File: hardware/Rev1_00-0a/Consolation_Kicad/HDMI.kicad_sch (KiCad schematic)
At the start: 13 parts, among them J1 0484050003, U3 AP2192AFGEG-7

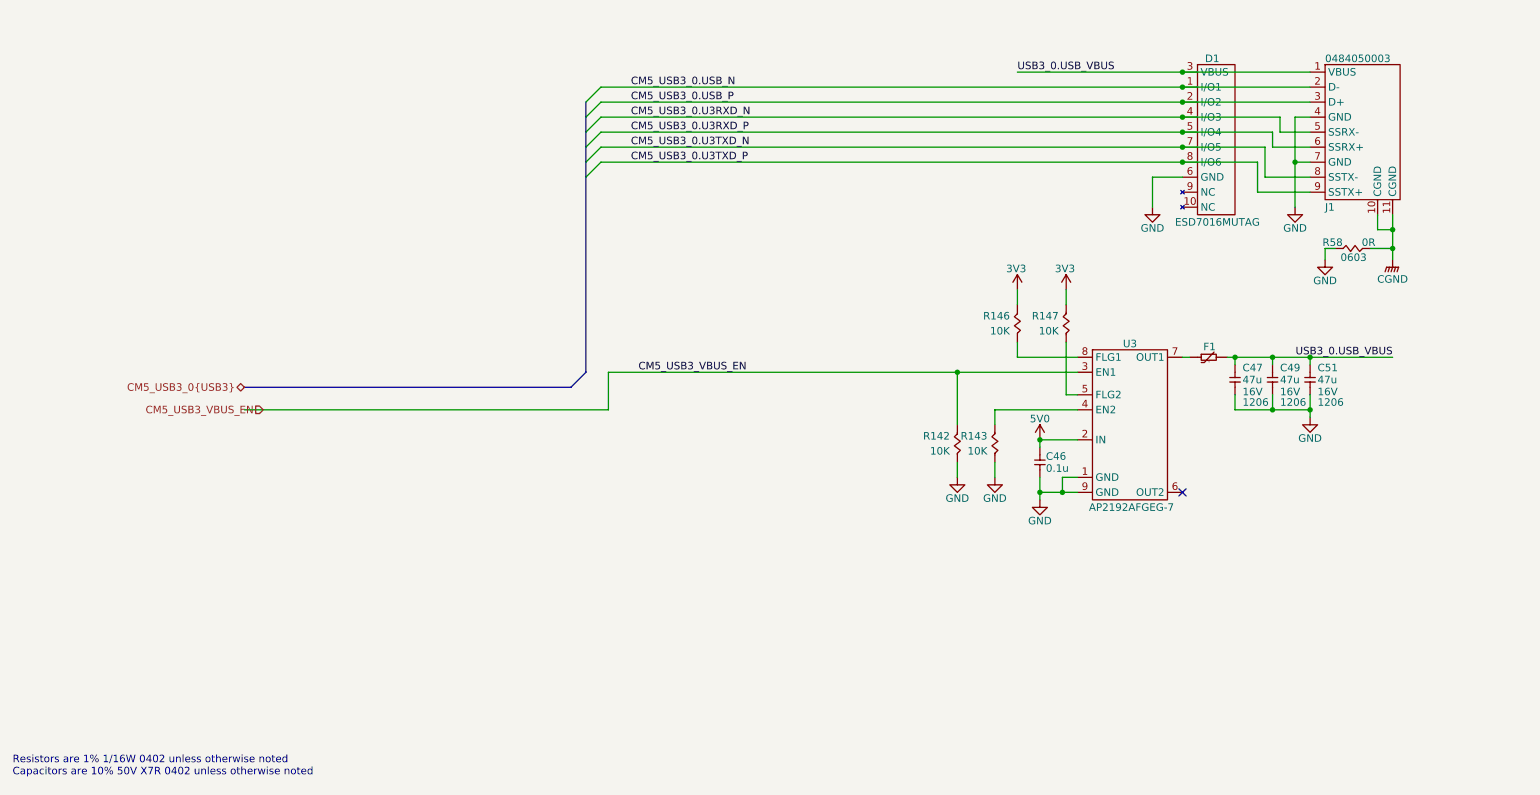
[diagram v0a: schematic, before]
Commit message: Add part number of codec to block diagram Add codec and hdmi schematic sheets
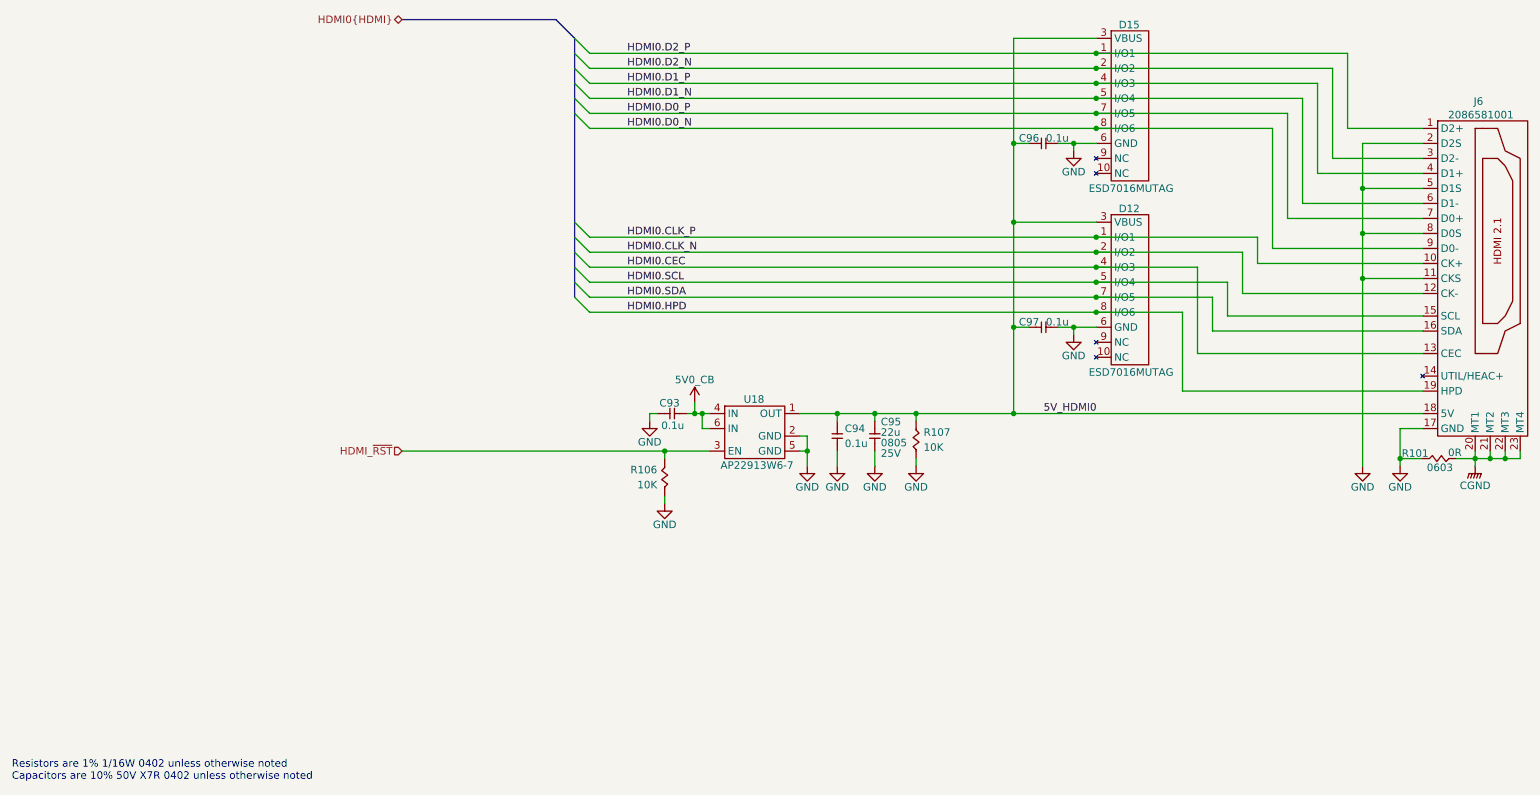
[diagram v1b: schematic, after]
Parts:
- removed C46: 0.1u, footprint:CAP_NONPOL_0402, symbol KicadCompDb:Capacitors/CAP_CER_SMT_00001
- removed C47, C49, C51: 47u, footprint:CAP_NONPOL_1206, symbol KicadCompDb:Capacitors/CAP_CER_SMT_00010
- removed D1: ESD7016MUTAG, footprint:UDFN8, symbol KicadCompDb:ESD Diodes/ESD_DIODE_00001
- removed F1: MINISMDC050F-2, footprint:PTC_1812, symbol KicadCompDb:PTC Resettable fuse/PTC_00001
- removed J1: 0484050003, footprint:0484050003, symbol KicadCompDb:Connector/CONN_00009
- removed R142, R143, R146, R147: 10K, footprint:RES_0402, symbol KicadCompDb:Resistors/RES_SMT_00013
- removed R58: 0R, footprint:RES_0603, symbol KicadCompDb:Resistors/RES_SMT_00021
- removed U3: AP2192AFGEG-7, footprint:U-DFN3030-8, symbol KicadCompDb:Load Switch/LOAD_SW_00002
- added C93, C94, C96, C97: 0.1u, footprint:CAP_NONPOL_0402, symbol KicadCompDb:Capacitors/CAP_CER_SMT_00001
- added C95: 22u, footprint:CAP_NONPOL_0805, symbol KicadCompDb:Capacitors/CAP_CER_SMT_00011
- added D12, D15: ESD7016MUTAG, footprint:UDFN8, symbol KicadCompDb:ESD Diodes/ESD_DIODE_00001
- added J6: 2086581001, footprint:2086581001, symbol KicadCompDb:Connector/CONN_00010
- added R101: 0R, footprint:RES_0603, symbol KicadCompDb:Resistors/RES_SMT_00021
- added R106, R107: 10K, footprint:RES_0402, symbol KicadCompDb:Resistors/RES_SMT_00013
- added U18: AP22913W6-7, footprint:SOT-23-6, symbol KicadCompDb:Load Switch/LOAD_SW_00001
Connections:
- net CGND: now also J6.20 (MT1), J6.21 (MT2), J6.22 (MT3), J6.23 (MT4), R101.1
- net GND: now also C93.1, C94.1, C95.1, C96.1, C97.1, D12.6 (GND), D15.6 (GND), J6.11 (CKS), J6.17 (GND), J6.2 (D2S), J6.5 (D1S), J6.8 (D0S), R101.2, R106.1, R107.1, U18.2 (GND), U18.5 (GND)
- new net 5V0_CB: C93.2, U18.4 (IN), U18.6 (IN)
- new net 5V_HDMI0: C94.2, C95.2, C96.2, C97.2, D12.3 (VBUS), D15.3 (VBUS), J6.18 (5V), R107.2, U18.1 (OUT)
- new net HDMI0.CEC: D12.4 (I/O3), J6.13 (CEC)
- new net HDMI0.CLK_N: D12.2 (I/O2), J6.12 (CK-)
- new net HDMI0.CLK_P: D12.1 (I/O1), J6.10 (CK+)
- new net HDMI0.D0_N: D15.8 (I/O6), J6.9 (D0-)
- new net HDMI0.D0_P: D15.7 (I/O5), J6.7 (D0+)
- new net HDMI0.D1_N: D15.5 (I/O4), J6.6 (D1-)
- new net HDMI0.D1_P: D15.4 (I/O3), J6.4 (D1+)
- new net HDMI0.D2_N: D15.2 (I/O2), J6.3 (D2-)
- new net HDMI0.D2_P: D15.1 (I/O1), J6.1 (D2+)
- new net HDMI0.HPD: D12.8 (I/O6), J6.19 (HPD)
- new net HDMI0.SCL: D12.5 (I/O4), J6.15 (SCL)
- new net HDMI0.SDA: D12.7 (I/O5), J6.16 (SDA)
- new net HDMI_~{RST}: R106.2, U18.3 (EN)
- no-connect marks 1 -> 0

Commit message: Update schematics, block diagram and pin mux (good progress G)
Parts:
- removed R101: 0R, footprint:RES_0603, symbol KicadCompDb:Resistors/RES_SMT_00021
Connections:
- net CGND is gone; now on net GND: J6.20 (MT1), J6.21 (MT2), J6.22 (MT3), J6.23 (MT4)
- net HDMI_~{RST} renamed ~{HDMI_RST}

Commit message: Update ConJoy L2 trigger (2-level trigger instead) Update ConJoy all output files accordingly
Work on Consolation preliminary placement
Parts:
- removed C96, C97: 0.1u, footprint:CAP_NONPOL_0402, symbol KicadCompDb:Capacitors/CAP_CER_SMT_00001
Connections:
- net 5V_HDMI0: no longer D12.3 (VBUS), D15.3 (VBUS)
- net GND: now also D12.3 (VBUS), D15.3 (VBUS)

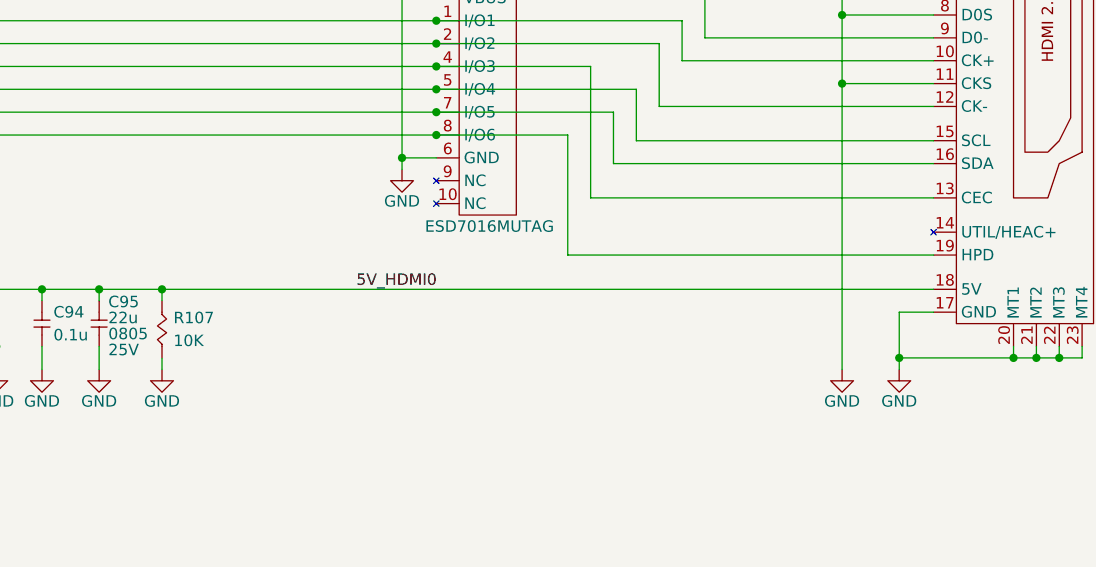
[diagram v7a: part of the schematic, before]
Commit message: Preliminary placement done Add test points to PCB
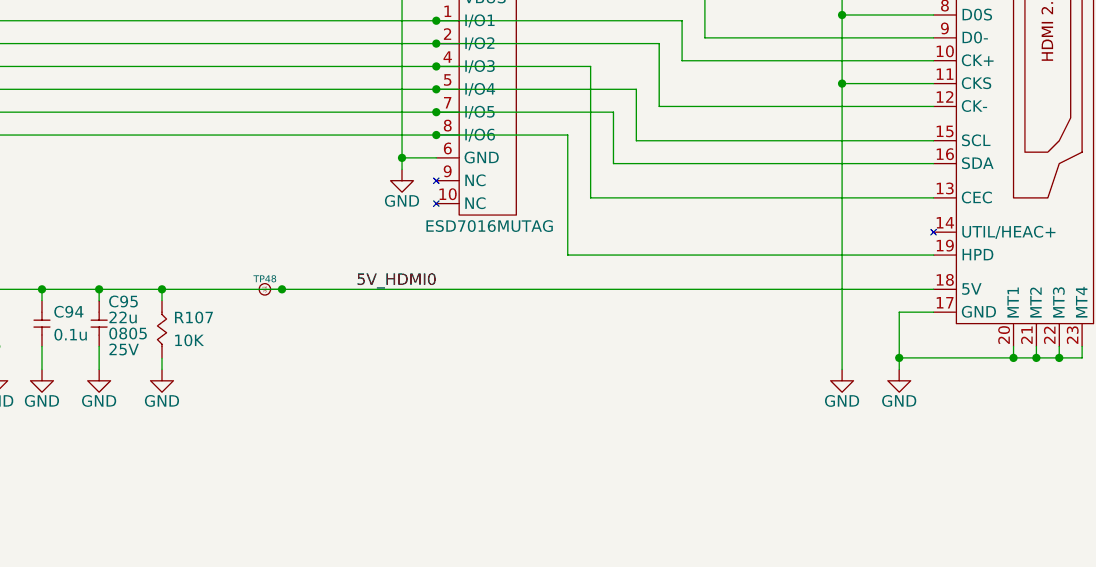
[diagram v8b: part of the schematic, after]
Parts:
- added TP48: 75 mils, footprint:SMT_TP_75_MILS, symbol KicadCompDb:Test Point/TP_00004
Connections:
- net 5V_HDMI0: now also TP48.1
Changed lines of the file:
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@@
 	(title_block
 		(title "Consolation [Console Emulation]")
-		(date "2026-08-29")
+		(date "2026-09-20")
 		(rev "1.00-0A")
 		(comment 1 "Jean-Francois Bilodeau")
@@
 	)
 	(junction
+		(at 179.07 110.49)
+		(diameter 0)
+		(color 0 0 0 0)
+	)
+	(junction
 		(at 241.3 87.63)
 		(diameter 0)
@@
 	(wire
 		(pts
-			(xy 165.735 110.49) (xy 251.46 110.49)
+			(xy 165.735 110.49) (xy 179.07 110.49)
 		)
 		(stroke
@@
 		(pts
 			(xy 241.3 87.63) (xy 241.3 119.38)
+		)
+		(stroke
+			(width 0)
+			(type default)
+		)
+	)
+	(wire
+		(pts
+			(xy 179.07 110.49) (xy 251.46 110.49)
 		)
 		(stroke
@@
 					(unit 1)
 				)
+			)
+		)
+	)
+	(symbol
+		(lib_id "KicadCompDb:Test Point/TP_00004")
+		(at 177.8 110.49 180)
+		(unit 1)
+		(body_style 1)
+		(exclude_from_sim no)
+		(in_bom yes)
+		(on_board yes)
+		(in_pos_files yes)
+		(dnp no)
+		(property "Reference" "TP48"
+			(at 175.895 109.347 0)
+			(show_name no)
+			(do_not_autoplace no)
+			(effects
+				(font
+					(size 0.762 0.762)
+				)
+				(justify right)
+			)
+		)
+		(property "Value" "75 mils"
+			(at 177.165 109.474 0)
+			(hide yes)
+			(show_name no)
+			(do_not_autoplace no)
+			(effects
+				(font
+					(size 0.762 0.762)
+				)
+			)
+		)
+		(property "Footprint" "footprint:SMT_TP_75_MILS"
+			(at 177.8 108.585 0)
+			(hide yes)
+			(show_name no)
+			(do_not_autoplace no)
+			(effects
+				(font
+					(size 1.27 1.27)
+				)
+			)
+		)
+		(property "Datasheet" "NA"
+			(at 177.8 110.49 0)
+			(hide yes)
+			(show_name no)
+			(do_not_autoplace no)
+			(effects
+				(font
+					(size 1.27 1.27)
+				)
+			)
+		)
+		(property "Description" "SMT TP 75 mils"
+			(at 177.8 110.49 0)
+			(hide yes)
+			(show_name no)
+			(do_not_autoplace no)
+			(effects
+				(font
+					(size 1.27 1.27)
+				)
+			)
+		)
+		(property "Dimensions" "75 mils"
+			(at 177.8 110.49 0)
+			(hide yes)
+			(show_name yes)
+			(do_not_autoplace no)
+			(effects
+				(font
+					(size 1.27 1.27)
+				)
+			)
+		)
+		(property "Distributor" "NA"
+			(at 177.8 110.49 0)
+			(hide yes)
+			(show_name yes)
+			(do_not_autoplace no)
+			(effects
+				(font
+					(size 1.27 1.27)
+				)
+			)
+		)
+		(property "Distributor Part Number" "NA"
+			(at 177.8 110.49 0)
+			(hide yes)
+			(show_name yes)
+			(do_not_autoplace no)
+			(effects
+				(font
+					(size 1.27 1.27)
+				)
+			)
+		)
+		(property "Manufacturer" "NA"
+			(at 177.8 110.49 0)
+			(hide yes)
+			(show_name yes)
+			(do_not_autoplace no)
+			(effects
+				(font
+					(size 1.27 1.27)
+				)
+			)
+		)
+		(property "Manufacturer Part Number" "NA"
+			(at 177.8 110.49 0)
+			(hide yes)
+			(show_name yes)
+			(do_not_autoplace no)
+			(effects
+				(font
+					(size 1.27 1.27)
+				)
+			)
+		)
+		(property "Operating Temperature" "NA"
+			(at 177.8 110.49 0)
+			(hide yes)
+			(show_name yes)
+			(do_not_autoplace no)
+			(effects
+				(font
+					(size 1.27 1.27)
+				)
+			)
+		)
+		(property "Package" "NA"
+			(at 177.8 110.49 0)
+			(hide yes)
+			(show_name yes)
+			(do_not_autoplace no)
+			(effects
+				(font
+					(size 1.27 1.27)
+				)
+			)
+		)
+		(property "Type" "SMT"
+			(at 177.8 110.49 0)
+			(hide yes)
+			(show_name yes)
+			(do_not_autoplace no)
+			(effects
+				(font
+					(size 1.27 1.27)
+				)
+			)
+		)
+		(pin "1"
+		)
+		(instances
+			(project "Consolation_Kicad"
+				(path "/b18b5a64-cfe0-4447-acaf-556f3c6e6513/c81e7ef2-aeaa-4a92-bec0-2bc97d679418"
+					(reference "TP48")
+					(unit 1)
+				)
